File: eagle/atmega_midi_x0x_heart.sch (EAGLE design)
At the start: 48 parts, among them J11_VCF_CUTOFF 22-23-2021, U1 ATMEGA328P_PDIP, U2 TLV2372IP, U3 DS1267S-010+DIP14

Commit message: using molex friction parts
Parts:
- D2: device diode:ZENER-DIODEDO34-7 -> diode:ZENER-DIODEDO35Z10
- MIDI_OUT_THRU, RES1, RES2, RES_POT: value (none) -> 22-23-2031; device con-lstb:MA03-1 -> con-molex:22-23-2031
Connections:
- net +5V: now also POWER_LED-1.S, RES_POT-1.S; no longer RES_POT.1
- net GND: now also MIDI_OUT_THRU-3.S, RES_POT-3.S; no longer MIDI_OUT_THRU.3, RES_POT.3
- net N$31: now also RES2-2.S; no longer RES1.2
- net N$32: now also RES2-1.S; no longer RES1.1
- net N$33: now also RES2-3.S; no longer RES1.3
- net N$34: now also RES1-2.S; no longer RES2.2
- net N$35: now also RES1-1.S; no longer RES2.1
- net N$36: now also RES1-3.S; no longer RES2.3
- net N$38: now also RES_POT-2.S; no longer RES_POT.2
- net N$39: now also MIDI_OUT_THRU-1.S; no longer MIDI_OUT_THRU.1
- net N$42: now also MIDI_OUT_THRU-2.S; no longer MIDI_OUT_THRU.2
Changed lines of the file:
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@@
 <part name="R6" library="rcl" deviceset="R-US_" device="0207/10" value="100k"/>
 <part name="U2" library="Texas Instruments_By_element14_Batch_1" deviceset="TLV2372IP" device=""/>
-<part name="RES1" library="con-lstb" deviceset="MA03-1" device=""/>
-<part name="RES2" library="con-lstb" deviceset="MA03-1" device=""/>
 <part name="P+8" library="supply1" deviceset="+5V" device=""/>
 <part name="GND13" library="supply1" deviceset="GND" device=""/>
-<part name="RES_POT" library="con-lstb" deviceset="MA03-1" device=""/>
 <part name="P+9" library="supply1" deviceset="+5V" device=""/>
 <part name="GND14" library="supply1" deviceset="GND" device=""/>
 <part name="R9" library="rcl" deviceset="R-US_" device="0207/10" value="220"/>
-<part name="MIDI_OUT_THRU" library="con-lstb" deviceset="MA03-1" device=""/>
 <part name="GND15" library="supply1" deviceset="GND" device=""/>
 <part name="R12" library="rcl" deviceset="R-US_" device="0207/10" value="2k4"/>
 <part name="U3" library="Maxim_By_element14_Batch_1" deviceset="DS1267S-010+" device="DIP14"/>
-<part name="D2" library="diode" deviceset="ZENER-DIODE" device="DO34-7" value="5V"/>
+<part name="D2" library="diode" deviceset="ZENER-DIODE" device="DO35Z10" value="5V"/>
 <part name="R13" library="rcl" deviceset="R-US_" device="0207/10" value="100"/>
 <part name="GND16" library="supply1" deviceset="GND" device=""/>
@@
 <part name="GATE_LED" library="con-molex" deviceset="22-23-2021" device=""/>
 <part name="POWER_LED" library="con-molex" deviceset="22-23-2021" device=""/>
+<part name="RES2" library="con-molex" deviceset="22-23-2031" device=""/>
+<part name="RES1" library="con-molex" deviceset="22-23-2031" device=""/>
+<part name="MIDI_OUT_THRU" library="con-molex" deviceset="22-23-2031" device=""/>
+<part name="RES_POT" library="con-molex" deviceset="22-23-2031" device=""/>
 </parts>
 <sheets>
@@
 <instance part="R6" gate="G$1" x="177.8" y="78.74"/>
 <instance part="U2" gate="A" x="149.86" y="88.9"/>
-<instance part="RES1" gate="G$1" x="208.28" y="33.02" rot="R180"/>
-<instance part="RES2" gate="G$1" x="208.28" y="20.32" rot="R180"/>
 <instance part="P+8" gate="1" x="162.56" y="60.96"/>
 <instance part="GND13" gate="1" x="157.48" y="7.62"/>
-<instance part="RES_POT" gate="G$1" x="88.9" y="63.5" rot="R180"/>
 <instance part="P+9" gate="1" x="81.28" y="73.66"/>
 <instance part="GND14" gate="1" x="81.28" y="50.8"/>
 <instance part="R9" gate="G$1" x="50.8" y="124.46"/>
-<instance part="MIDI_OUT_THRU" gate="G$1" x="73.66" y="121.92" rot="R180"/>
 <instance part="GND15" gate="1" x="66.04" y="111.76"/>
 <instance part="R12" gate="G$1" x="40.64" y="101.6" rot="R90"/>
@@
 <instance part="POWER_LED" gate="-1" x="185.42" y="111.76" rot="MR180"/>
 <instance part="POWER_LED" gate="-2" x="185.42" y="109.22" rot="MR180"/>
+<instance part="RES2" gate="-1" x="203.2" y="35.56"/>
+<instance part="RES2" gate="-2" x="203.2" y="33.02"/>
+<instance part="RES2" gate="-3" x="203.2" y="30.48"/>
+<instance part="RES1" gate="-1" x="203.2" y="22.86"/>
+<instance part="RES1" gate="-2" x="203.2" y="20.32"/>
+<instance part="RES1" gate="-3" x="203.2" y="17.78"/>
+<instance part="MIDI_OUT_THRU" gate="-1" x="68.58" y="124.46"/>
+<instance part="MIDI_OUT_THRU" gate="-2" x="68.58" y="121.92"/>
+<instance part="MIDI_OUT_THRU" gate="-3" x="68.58" y="119.38"/>
+<instance part="RES_POT" gate="-1" x="83.82" y="66.04"/>
+<instance part="RES_POT" gate="-2" x="83.82" y="63.5"/>
+<instance part="RES_POT" gate="-3" x="83.82" y="60.96"/>
 </instances>
 <busses>
@@
 </segment>
 <segment>
-<pinref part="RES_POT" gate="G$1" pin="1"/>
 <pinref part="P+9" gate="1" pin="+5V"/>
 <wire x1="81.28" y1="71.12" x2="81.28" y2="66.04" width="0.1524" layer="91"/>
+<pinref part="RES_POT" gate="-1" pin="S"/>
 </segment>
 <segment>
@@
 <wire x1="177.8" y1="119.38" x2="177.8" y2="111.76" width="0.1524" layer="91"/>
 <wire x1="177.8" y1="111.76" x2="182.88" y2="111.76" width="0.1524" layer="91"/>
+<pinref part="POWER_LED" gate="-1" pin="S"/>
 </segment>
 </net>
@@
 </segment>
 <segment>
-<pinref part="RES_POT" gate="G$1" pin="3"/>
 <pinref part="GND14" gate="1" pin="GND"/>
 <wire x1="81.28" y1="53.34" x2="81.28" y2="60.96" width="0.1524" layer="91"/>
-</segment>
-<segment>
-<pinref part="MIDI_OUT_THRU" gate="G$1" pin="3"/>
+<pinref part="RES_POT" gate="-3" pin="S"/>
+</segment>
+<segment>
 <pinref part="GND15" gate="1" pin="GND"/>
 <wire x1="66.04" y1="114.3" x2="66.04" y2="119.38" width="0.1524" layer="91"/>
+<pinref part="MIDI_OUT_THRU" gate="-3" pin="S"/>
 </segment>
 <segment>
@@
 <net name="N$31" class="0">
 <segment>
-<pinref part="RES1" gate="G$1" pin="2"/>
 <wire x1="198.12" y1="33.02" x2="200.66" y2="33.02" width="0.1524" layer="91"/>
 <pinref part="U3" gate="A" pin="W1"/>
+<pinref part="RES2" gate="-2" pin="S"/>
 </segment>
 </net>
 <net name="N$32" class="0">
 <segment>
-<pinref part="RES1" gate="G$1" pin="1"/>
 <wire x1="198.12" y1="35.56" x2="200.66" y2="35.56" width="0.1524" layer="91"/>
 <pinref part="U3" gate="A" pin="H1"/>
+<pinref part="RES2" gate="-1" pin="S"/>
 </segment>
 </net>
 <net name="N$34" class="0">
 <segment>
-<pinref part="RES2" gate="G$1" pin="2"/>
 <wire x1="198.12" y1="20.32" x2="200.66" y2="20.32" width="0.1524" layer="91"/>
 <pinref part="U3" gate="A" pin="W0"/>
+<pinref part="RES1" gate="-2" pin="S"/>
 </segment>
 </net>
 <net name="N$35" class="0">
 <segment>
-<pinref part="RES2" gate="G$1" pin="1"/>
 <wire x1="198.12" y1="22.86" x2="200.66" y2="22.86" width="0.1524" layer="91"/>
 <pinref part="U3" gate="A" pin="H0"/>
+<pinref part="RES1" gate="-1" pin="S"/>
 </segment>
 </net>
 <net name="N$36" class="0">
 <segment>
-<pinref part="RES2" gate="G$1" pin="3"/>
 <wire x1="198.12" y1="17.78" x2="200.66" y2="17.78" width="0.1524" layer="91"/>
 <pinref part="U3" gate="A" pin="L0"/>
+<pinref part="RES1" gate="-3" pin="S"/>
 </segment>
 </net>
@@
 <net name="N$38" class="0">
 <segment>
-<pinref part="RES_POT" gate="G$1" pin="2"/>
 <pinref part="U1" gate="G$1" pin="PC4(ADC4/SDA)"/>
 <wire x1="81.28" y1="63.5" x2="43.18" y2="63.5" width="0.1524" layer="91"/>
+<pinref part="RES_POT" gate="-2" pin="S"/>
 </segment>
 </net>
 <net name="N$39" class="0">
 <segment>
-<pinref part="MIDI_OUT_THRU" gate="G$1" pin="1"/>
 <pinref part="R9" gate="G$1" pin="2"/>
 <wire x1="55.88" y1="124.46" x2="66.04" y2="124.46" width="0.1524" layer="91"/>
+<pinref part="MIDI_OUT_THRU" gate="-1" pin="S"/>
 </segment>
 </net>
@@
 <wire x1="43.18" y1="48.26" x2="58.42" y2="48.26" width="0.1524" layer="91"/>
 <wire x1="58.42" y1="48.26" x2="58.42" y2="121.92" width="0.1524" layer="91"/>
-<pinref part="MIDI_OUT_THRU" gate="G$1" pin="2"/>
 <wire x1="58.42" y1="121.92" x2="66.04" y2="121.92" width="0.1524" layer="91"/>
+<pinref part="MIDI_OUT_THRU" gate="-2" pin="S"/>
 </segment>
 </net>
@@
 <net name="N$33" class="0">
 <segment>
-<pinref part="RES1" gate="G$1" pin="3"/>
 <pinref part="U3" gate="A" pin="L1"/>
 <wire x1="200.66" y1="30.48" x2="198.12" y2="30.48" width="0.1524" layer="91"/>
-</segment>
-</net>
+<pinref part="RES2" gate="-3" pin="S"/>
+</segment>
+</net>

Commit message: 90pct auto
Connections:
- net +5V: now also U1.AVCC; no longer U1.AREF
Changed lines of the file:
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@@
 <segment>
 <pinref part="U1" gate="G$1" pin="VCC"/>
-<wire x1="-5.08" y1="66.04" x2="-7.62" y2="66.04" width="0.1524" layer="91"/>
-<wire x1="-7.62" y1="66.04" x2="-12.7" y2="66.04" width="0.1524" layer="91"/>
-<wire x1="-12.7" y1="66.04" x2="-12.7" y2="76.2" width="0.1524" layer="91"/>
+<wire x1="-5.08" y1="66.04" x2="-12.7" y2="66.04" width="0.1524" layer="91"/>
+<wire x1="-12.7" y1="66.04" x2="-12.7" y2="68.58" width="0.1524" layer="91"/>
+<wire x1="-12.7" y1="68.58" x2="-12.7" y2="76.2" width="0.1524" layer="91"/>
 <wire x1="-12.7" y1="76.2" x2="-25.4" y2="76.2" width="0.1524" layer="91"/>
 <pinref part="R1" gate="G$1" pin="1"/>
@@
 <wire x1="-25.4" y1="71.12" x2="-25.4" y2="76.2" width="0.1524" layer="91"/>
 <junction x="-25.4" y="76.2"/>
-<pinref part="U1" gate="G$1" pin="AREF"/>
-<wire x1="-5.08" y1="58.42" x2="-7.62" y2="58.42" width="0.1524" layer="91"/>
-<wire x1="-7.62" y1="58.42" x2="-7.62" y2="66.04" width="0.1524" layer="91"/>
-<junction x="-7.62" y="66.04"/>
+<pinref part="U1" gate="G$1" pin="AVCC"/>
+<wire x1="-5.08" y1="68.58" x2="-12.7" y2="68.58" width="0.1524" layer="91"/>
+<junction x="-12.7" y="68.58"/>
 </segment>
 <segment>

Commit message: possibly routed
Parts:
- C7: device rcl:CPOL-USB45181A -> rcl:CPOL-USB45181B
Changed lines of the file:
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@@
 <part name="P-1" library="supply1" deviceset="-12V" device=""/>
 <part name="P-2" library="supply1" deviceset="-12V" device=""/>
-<part name="C7" library="rcl" deviceset="CPOL-US" device="B45181A" value="10u"/>
+<part name="C7" library="rcl" deviceset="CPOL-US" device="B45181B" value="10u"/>
 <part name="GND17" library="supply1" deviceset="GND" device=""/>
 <part name="R14" library="rcl" deviceset="R-US_" device="0207/10" value="1k"/>
@@
 </segment>
 <segment>
-<pinref part="P+3" gate="1" pin="+5V"/>
-<pinref part="MIDI_CH" gate="G$1" pin="E"/>
-<wire x1="53.34" y1="96.52" x2="53.34" y2="99.06" width="0.1524" layer="91"/>
-</segment>
-<segment>
 <pinref part="P+8" gate="1" pin="+5V"/>
 <wire x1="162.56" y1="55.88" x2="162.56" y2="58.42" width="0.1524" layer="91"/>
@@
 <wire x1="177.8" y1="111.76" x2="182.88" y2="111.76" width="0.1524" layer="91"/>
 <pinref part="POWER_LED" gate="-1" pin="S"/>
+</segment>
+<segment>
+<pinref part="P+3" gate="1" pin="+5V"/>
+<pinref part="MIDI_CH" gate="G$1" pin="E"/>
+<wire x1="53.34" y1="96.52" x2="53.34" y2="99.06" width="0.1524" layer="91"/>
 </segment>
 </net>
@@
 <net name="N$19" class="0">
 <segment>
+<pinref part="U1" gate="G$1" pin="PC0(ADC0)"/>
+<wire x1="48.26" y1="73.66" x2="43.18" y2="73.66" width="0.1524" layer="91"/>
 <pinref part="MIDI_CH" gate="G$1" pin="S"/>
-<pinref part="U1" gate="G$1" pin="PC0(ADC0)"/>
 <wire x1="48.26" y1="88.9" x2="48.26" y2="73.66" width="0.1524" layer="91"/>
-<wire x1="48.26" y1="73.66" x2="43.18" y2="73.66" width="0.1524" layer="91"/>
 </segment>
 </net>
@@
 </segment>
 <segment>
-<pinref part="MIDI_CH" gate="G$1" pin="A"/>
-<wire x1="53.34" y1="81.28" x2="53.34" y2="78.74" width="0.1524" layer="91"/>
-<pinref part="GND5" gate="1" pin="GND"/>
-</segment>
-<segment>
 <wire x1="111.76" y1="53.34" x2="111.76" y2="63.5" width="0.1524" layer="91"/>
 <pinref part="R8" gate="G$1" pin="1"/>
@@
 <wire x1="208.28" y1="104.14" x2="210.82" y2="104.14" width="0.1524" layer="91"/>
 </segment>
+<segment>
+<pinref part="GND5" gate="1" pin="GND"/>
+<pinref part="MIDI_CH" gate="G$1" pin="A"/>
+<wire x1="53.34" y1="81.28" x2="53.34" y2="78.74" width="0.1524" layer="91"/>
+</segment>
 </net>
 <net name="N$24" class="0">
@@
 <segment>
 <pinref part="U1" gate="G$1" pin="PD1(TXD)"/>
-<wire x1="43.18" y1="48.26" x2="58.42" y2="48.26" width="0.1524" layer="91"/>
-<wire x1="58.42" y1="48.26" x2="58.42" y2="121.92" width="0.1524" layer="91"/>
-<wire x1="58.42" y1="121.92" x2="66.04" y2="121.92" width="0.1524" layer="91"/>
+<wire x1="43.18" y1="48.26" x2="60.96" y2="48.26" width="0.1524" layer="91"/>
+<wire x1="60.96" y1="48.26" x2="60.96" y2="121.92" width="0.1524" layer="91"/>
+<wire x1="60.96" y1="121.92" x2="66.04" y2="121.92" width="0.1524" layer="91"/>
 <pinref part="MIDI_OUT_THRU" gate="-2" pin="S"/>
 </segment>

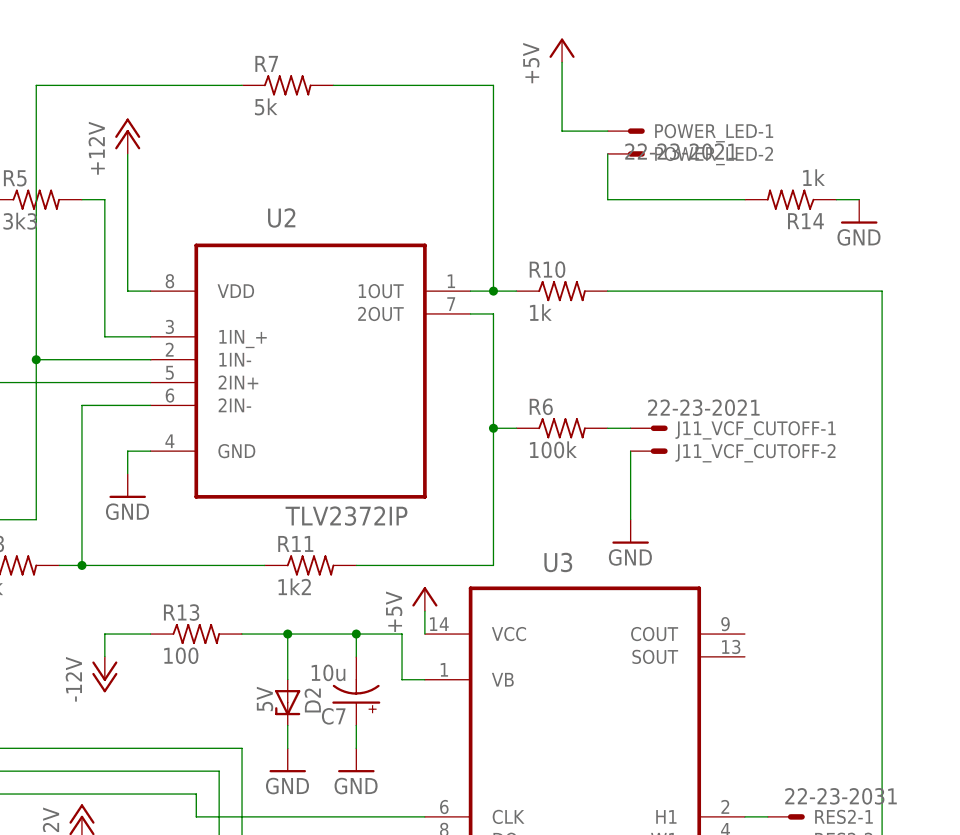
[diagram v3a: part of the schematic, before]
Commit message: reversed resonance and fixed a couple of pins
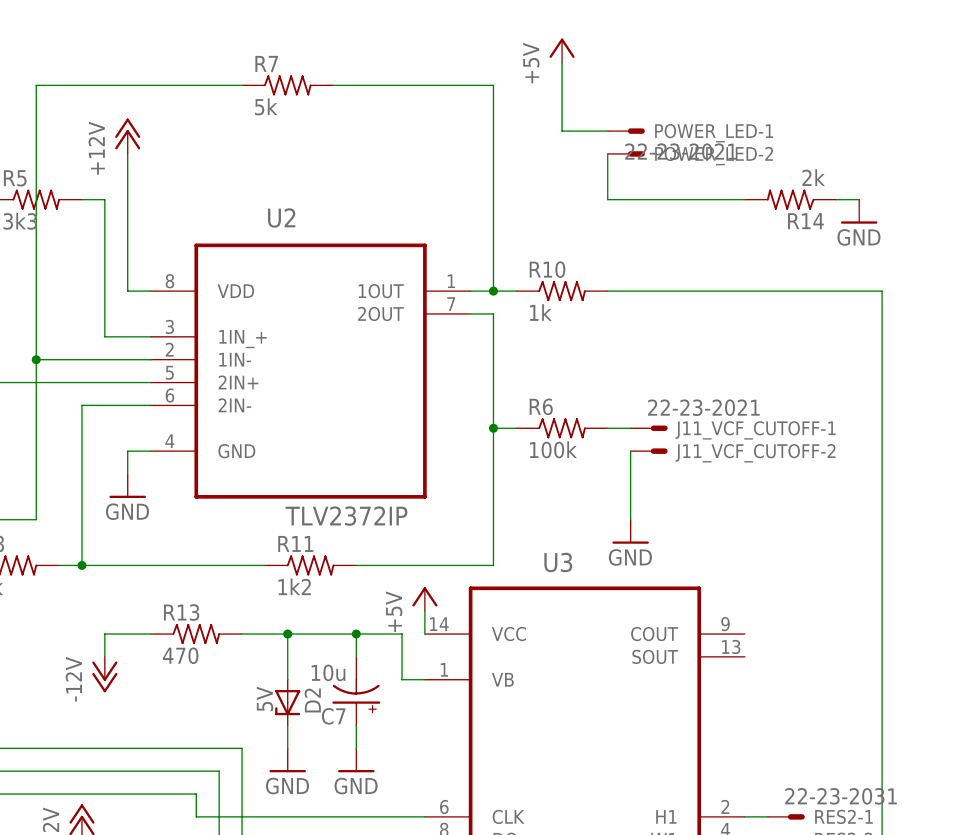
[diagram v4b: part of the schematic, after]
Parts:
- R13: value 100 -> 470
- R14: value 1k -> 2k
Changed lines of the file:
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@@
 <?xml version="1.0" encoding="utf-8"?>
 <!DOCTYPE eagle SYSTEM "eagle.dtd">
-<eagle version="7.2.0">
+<eagle version="7.1.0">
 <drawing>
 <settings>
@@
 <grid distance="0.1" unitdist="inch" unit="inch" style="lines" multiple="1" display="no" altdistance="0.01" altunitdist="inch" altunit="inch"/>
 <layers>
-<layer number="1" name="Top" color="4" fill="1" visible="yes" active="no"/>
-<layer number="16" name="Bottom" color="1" fill="1" visible="yes" active="no"/>
-<layer number="17" name="Pads" color="2" fill="1" visible="yes" active="no"/>
-<layer number="18" name="Vias" color="2" fill="1" visible="yes" active="no"/>
-<layer number="19" name="Unrouted" color="6" fill="1" visible="yes" active="no"/>
-<layer number="20" name="Dimension" color="15" fill="1" visible="yes" active="no"/>
-<layer number="21" name="tPlace" color="7" fill="1" visible="yes" active="no"/>
-<layer number="22" name="bPlace" color="7" fill="1" visible="yes" active="no"/>
-<layer number="23" name="tOrigins" color="15" fill="1" visible="yes" active="no"/>
-<layer number="24" name="bOrigins" color="15" fill="1" visible="yes" active="no"/>
-<layer number="25" name="tNames" color="7" fill="1" visible="yes" active="no"/>
-<layer number="26" name="bNames" color="7" fill="1" visible="yes" active="no"/>
-<layer number="27" name="tValues" color="7" fill="1" visible="yes" active="no"/>
-<layer number="28" name="bValues" color="7" fill="1" visible="yes" active="no"/>
+<layer number="1" name="Top" color="4" fill="1" visible="no" active="no"/>
+<layer number="16" name="Bottom" color="1" fill="1" visible="no" active="no"/>
+<layer number="17" name="Pads" color="2" fill="1" visible="no" active="no"/>
+<layer number="18" name="Vias" color="2" fill="1" visible="no" active="no"/>
+<layer number="19" name="Unrouted" color="6" fill="1" visible="no" active="no"/>
+<layer number="20" name="Dimension" color="15" fill="1" visible="no" active="no"/>
+<layer number="21" name="tPlace" color="7" fill="1" visible="no" active="no"/>
+<layer number="22" name="bPlace" color="7" fill="1" visible="no" active="no"/>
+<layer number="23" name="tOrigins" color="15" fill="1" visible="no" active="no"/>
+<layer number="24" name="bOrigins" color="15" fill="1" visible="no" active="no"/>
+<layer number="25" name="tNames" color="7" fill="1" visible="no" active="no"/>
+<layer number="26" name="bNames" color="7" fill="1" visible="no" active="no"/>
+<layer number="27" name="tValues" color="7" fill="1" visible="no" active="no"/>
+<layer number="28" name="bValues" color="7" fill="1" visible="no" active="no"/>
 <layer number="29" name="tStop" color="7" fill="3" visible="no" active="no"/>
 <layer number="30" name="bStop" color="7" fill="6" visible="no" active="no"/>
@@
 <layer number="35" name="tGlue" color="7" fill="4" visible="no" active="no"/>
 <layer number="36" name="bGlue" color="7" fill="5" visible="no" active="no"/>
-<layer number="37" name="tTest" color="7" fill="1" visible="yes" active="no"/>
-<layer number="38" name="bTest" color="7" fill="1" visible="yes" active="no"/>
+<layer number="37" name="tTest" color="7" fill="1" visible="no" active="no"/>
+<layer number="38" name="bTest" color="7" fill="1" visible="no" active="no"/>
 <layer number="39" name="tKeepout" color="4" fill="11" visible="no" active="no"/>
 <layer number="40" name="bKeepout" color="1" fill="11" visible="no" active="no"/>
@@
 <layer number="44" name="Drills" color="7" fill="1" visible="no" active="no"/>
 <layer number="45" name="Holes" color="7" fill="1" visible="no" active="no"/>
-<layer number="46" name="Milling" color="3" fill="1" visible="yes" active="no"/>
-<layer number="47" name="Measures" color="7" fill="1" visible="yes" active="no"/>
-<layer number="48" name="Document" color="7" fill="1" visible="yes" active="no"/>
-<layer number="49" name="Reference" color="7" fill="1" visible="yes" active="no"/>
-<layer number="50" name="dxf" color="7" fill="1" visible="yes" active="no"/>
-<layer number="51" name="tDocu" color="7" fill="1" visible="yes" active="no"/>
-<layer number="52" name="bDocu" color="7" fill="1" visible="yes" active="no"/>
-<layer number="53" name="tGND_GNDA" color="7" fill="9" visible="yes" active="no"/>
-<layer number="54" name="bGND_GNDA" color="1" fill="9" visible="yes" active="no"/>
-<layer number="56" name="wert" color="7" fill="1" visible="yes" active="no"/>
-<layer number="57" name="tCAD" color="7" fill="1" visible="yes" active="no"/>
-<layer number="59" name="tCarbon" color="7" fill="1" visible="yes" active="no"/>
-<layer number="60" name="bCarbon" color="7" fill="1" visible="yes" active="no"/>
+<layer number="46" name="Milling" color="3" fill="1" visible="no" active="no"/>
+<layer number="47" name="Measures" color="7" fill="1" visible="no" active="no"/>
+<layer number="48" name="Document" color="7" fill="1" visible="no" active="no"/>
+<layer number="49" name="Reference" color="7" fill="1" visible="no" active="no"/>
+<layer number="50" name="dxf" color="7" fill="1" visible="no" active="no"/>
+<layer number="51" name="tDocu" color="7" fill="1" visible="no" active="no"/>
+<layer number="52" name="bDocu" color="7" fill="1" visible="no" active="no"/>
+<layer number="53" name="tGND_GNDA" color="7" fill="9" visible="no" active="no"/>
+<layer number="54" name="bGND_GNDA" color="1" fill="9" visible="no" active="no"/>
+<layer number="56" name="wert" color="7" fill="1" visible="no" active="no"/>
+<layer number="57" name="tCAD" color="7" fill="1" visible="no" active="no"/>
+<layer number="59" name="tCarbon" color="7" fill="1" visible="no" active="no"/>
+<layer number="60" name="bCarbon" color="7" fill="1" visible="no" active="no"/>
 <layer number="90" name="Modules" color="5" fill="1" visible="yes" active="yes"/>
 <layer number="91" name="Nets" color="2" fill="1" visible="yes" active="yes"/>
@@
 <part name="U3" library="Maxim_By_element14_Batch_1" deviceset="DS1267S-010+" device="DIP14"/>
 <part name="D2" library="diode" deviceset="ZENER-DIODE" device="DO35Z10" value="5V"/>
-<part name="R13" library="rcl" deviceset="R-US_" device="0207/10" value="100"/>
+<part name="R13" library="rcl" deviceset="R-US_" device="0207/10" value="470"/>
 <part name="GND16" library="supply1" deviceset="GND" device=""/>
 <part name="U$1" library="adafruit" deviceset="FB" device=""/>
@@
 <part name="C7" library="rcl" deviceset="CPOL-US" device="B45181B" value="10u"/>
 <part name="GND17" library="supply1" deviceset="GND" device=""/>
-<part name="R14" library="rcl" deviceset="R-US_" device="0207/10" value="1k"/>
+<part name="R14" library="rcl" deviceset="R-US_" device="0207/10" value="2k"/>
 <part name="P+10" library="supply1" deviceset="+5V" device=""/>
 <part name="GND18" library="supply1" deviceset="GND" device=""/>
